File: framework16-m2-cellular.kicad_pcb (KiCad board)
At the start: 4 copper layers, 118.7 x 72.5 mm, 88 parts, among them J1 M.2 Socket B-Key (2199230-3), J10 MHF4L (20579-001E), J11 SIM Card, J12 Fan 1, J13 Fan 2, J2 u.FL, J3 MHF4L (20579-001E), J5 u.FL, J6 MHF4L (20579-001E), J7 u.FL, J8 MHF4L (20579-001E), J9 u.FL, Q1 NPN, U1 BR24G32FVT-3, U2 TCA9534, U3 74LVC1G11, U4 LTC6994xS6-1, U5 TPS628304ARZER

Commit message: Version v1.1
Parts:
- added R9: 1K, Resistor_SMD:R_0603_1608Metric, F.Cu at (119.2, 97.0)
- added TP11: TestPoint, TestPoint:TestPoint_Pad_D1.0mm, F.Cu at (104.0, 91.0)
- added TP12: TestPoint, TestPoint:TestPoint_Pad_D1.0mm, F.Cu at (114.0, 124.0)
- added TP15: TestPoint, TestPoint:TestPoint_Pad_D1.0mm, F.Cu at (110.0, 124.0)
- moved TP13 38.4 mm to (112.0, 124.0)
- moved U4 22.1 mm to (102.0, 94.2)
- moved C16 22.1 mm to (105.0, 94.2)
- moved R14 22.1 mm to (104.3, 96.7)
- moved R16 22.1 mm to (101.3, 96.7)
- moved R17 22.1 mm to (99.0, 95.2)
- moved TP10 16.7 mm to (98.5, 92.5)
- moved R23 12.6 mm to (160.5, 137.5), turned to -90 degrees
- moved D1 2.50 mm to (146.0, 83.4)
- moved D3 2.50 mm to (149.0, 83.4)
- moved R1 2.50 mm to (144.0, 83.7)
- moved R7 2.50 mm to (151.0, 83.7)
- moved TP4 1.00 mm to (104.5, 111.2)
- moved C21 0.75 mm to (108.8, 89.5)
- moved C22 0.75 mm to (113.5, 87.5)
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- renumbered R7 to R1, R9 to R10, R10 to R11, R11 to R12, R12 to R13, R13 to R14, R14 to R15, R15 to R16, R16 to R17, R17 to R18, R18 to R19, R19 to R20, R20 to R21, R21 to R22, R22 to R23, R23 to R24, R1 to R7, TP11 to TP13, TP12 to TP14
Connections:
- Q1 pad 1: /RESET -> Net-(Q1-B)
- R10 pad 1: /RESET -> Net-(Q1-B)
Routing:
- net Net-(J4-ID0): track 14.6 -> 2.62 mm, vias 2 -> 0
- net /MODEM_ON: track 95.2 -> 106.3 mm, vias 4 -> 5
- net Net-(J1-GPIO_9/DAS/~{DSS}/~{LED1}): track 40.9 -> 50.8 mm
- net +3.3V: track 194.2 -> 188.0 mm
- net GND: track 379.5 -> 383.7 mm, vias 7 -> 26
- net /RESET: track 30.9 -> 26.7 mm
- net Net-(Q1-B): track 0.00 -> 3.85 mm
- net Net-(J13-Pin_3): track 48.6 -> 50.9 mm
- net +3.7V_MODEM: track 118.5 -> 116.3 mm
- net /~{INT}: track 127.8 -> 129.7 mm
- net /RST: track 40.7 -> 42.6 mm
- net /D+: track 42.1 -> 43.8 mm, vias 2 -> 3
- net /D-: track 43.7 -> 45.4 mm, vias 2 -> 3
- net Net-(J12-Pin_3): track 51.5 -> 53.1 mm
- net Net-(J4-12V_FAN): track 19.3 -> 20.9 mm
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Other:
- board text added: "Framework 16 M.2 Cellular Module ${VERSION}"
- board text removed: "FW16 5G Module v1.0"

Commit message: Bunch of improvements for v1.1
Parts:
- added HS1: M.2 Thermal Pads, FW16Cellular:Thermal Pad, F.Cu at (186.0, 94.8)
- added HS1: M.2 Thermal Pads, FW16Cellular:Thermal Pad, F.Cu at (176.0, 113.8)
- added HS1: M.2 Thermal Pads, FW16Cellular:Thermal Pad, F.Cu at (186.0, 113.8)
- added HS1: M.2 Thermal Pads, FW16Cellular:Thermal Pad, F.Cu at (166.0, 104.2)
- added HS1: M.2 Thermal Pads, FW16Cellular:Thermal Pad, F.Cu at (156.0, 94.8)
- added HS1: M.2 Thermal Pads, FW16Cellular:Thermal Pad, F.Cu at (176.0, 94.8)
- added HS1: M.2 Thermal Pads, FW16Cellular:Thermal Pad, F.Cu at (166.0, 113.8)
- added HS1: M.2 Thermal Pads, FW16Cellular:Thermal Pad, F.Cu at (156.0, 113.8)
- added HS1: M.2 Thermal Pads, FW16Cellular:Thermal Pad, F.Cu at (166.0, 94.8)
- added HS1: M.2 Thermal Pads, FW16Cellular:Thermal Pad, F.Cu at (156.0, 104.2)
- J2, J5, J7, J9: value u.FL -> MHF4L (20579-001E); footprint FW16Cellular:CONN_U.FL-R-SMT10_HIR -> FW16Cellular:CONN_20579-001E_IPX
- moved J2 96.9 mm to (114.0, 72.5), turned to 0 degrees
- moved J5 92.9 mm to (120.0, 72.5), turned to 0 degrees
- moved J3 91.2 mm to (114.0, 75.0), turned to 180 degrees
- moved J7 89.7 mm to (126.0, 72.5), turned to 0 degrees
- moved J9 87.4 mm to (132.0, 72.5), turned to 0 degrees
- moved J6 87.1 mm to (120.0, 75.0), turned to 180 degrees
- moved J8 83.9 mm to (126.0, 75.0), turned to 180 degrees
- moved J10 81.6 mm to (132.0, 75.0), turned to 180 degrees
- moved D1 4.03 mm to (142.0, 83.9)
- moved D3 4.03 mm to (145.0, 83.9)
- moved R1 4.03 mm to (140.0, 84.2)
- moved R7 4.03 mm to (147.0, 84.2)
- moved H1 1.00 mm to (176.0, 104.2)
- moved H2 1.00 mm to (186.0, 104.2)
- moved L1 0.25 mm to (166.0, 126.5)
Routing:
- net GND: track 383.7 -> 351.5 mm
- net Net-(J1-GPIO_9/DAS/~{DSS}/~{LED1}): track 50.8 -> 37.9 mm
- net /VCC: track 51.9 -> 57.8 mm
- net /RST: track 42.6 -> 48.5 mm
- net /DATA: track 39.1 -> 44.9 mm
- net /CLK: track 38.5 -> 44.4 mm
- net /~{CLKREQ}: track 46.3 -> 51.6 mm
- net /~{RST}: track 43.6 -> 47.1 mm
- net /MODEM_ON: track 106.3 -> 109.6 mm
- net /~{W_DISABLE1}: track 58.6 -> 61.7 mm
- net /REFCLKP: track 62.0 -> 64.9 mm
- net /REFCLKN: track 62.0 -> 64.9 mm
- net Net-(J1-~{FULL_CARD_POWER_OFF}): track 51.6 -> 54.2 mm
- net /~{INT}: track 129.7 -> 128.5 mm
- net +3.7V_MODEM: track 116.3 -> 115.0 mm
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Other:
- board text added: "EC ON"
- board text added: "FW Laptop 16 Expansion Bay M.2 5G Module ${VERSION}"
- board text removed: "Framework 16 M.2 Cellular Module ${VERSION}"

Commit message: Fixes from v1.1
TODO: check the orientation of the fan headers
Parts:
- C13, C5: footprint Capacitor_SMD:CP_Elec_8x10 -> Capacitor_SMD:CP_Elec_6.3x5.4
- J12, J13: footprint FW16Cellular:A1001WR-S-04P -> FW16Cellular:AFC30-S04FCC-00
- moved C5 0.25 mm to (126.0, 120.0)
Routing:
- net GND: track 351.5 -> 339.2 mm
- net +12V_FAN: track 104.4 -> 105.9 mm
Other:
- board text added: "EC CTRL"
- board text removed: "EC ON"

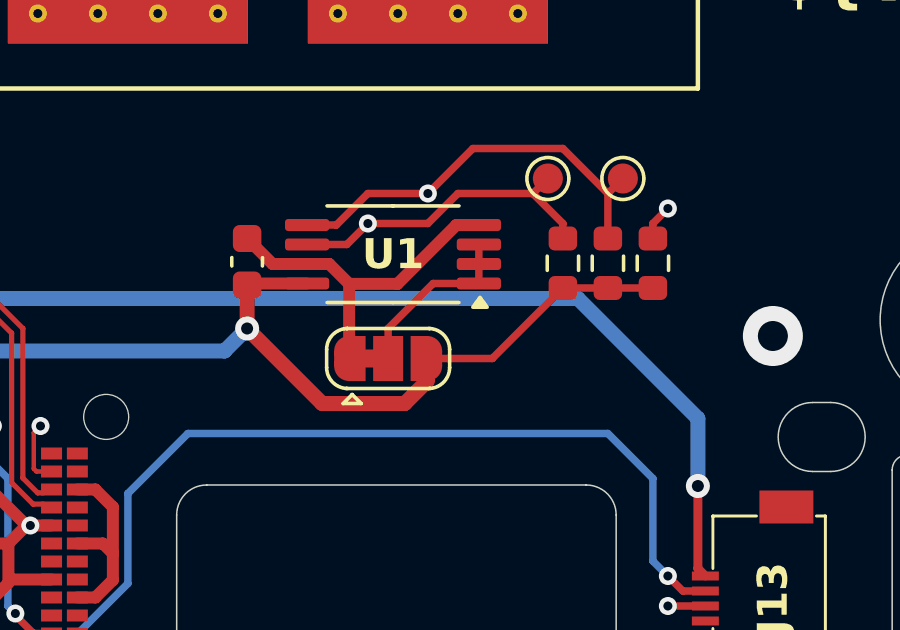
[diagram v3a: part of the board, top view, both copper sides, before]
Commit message: Remove EEPROM address jumper
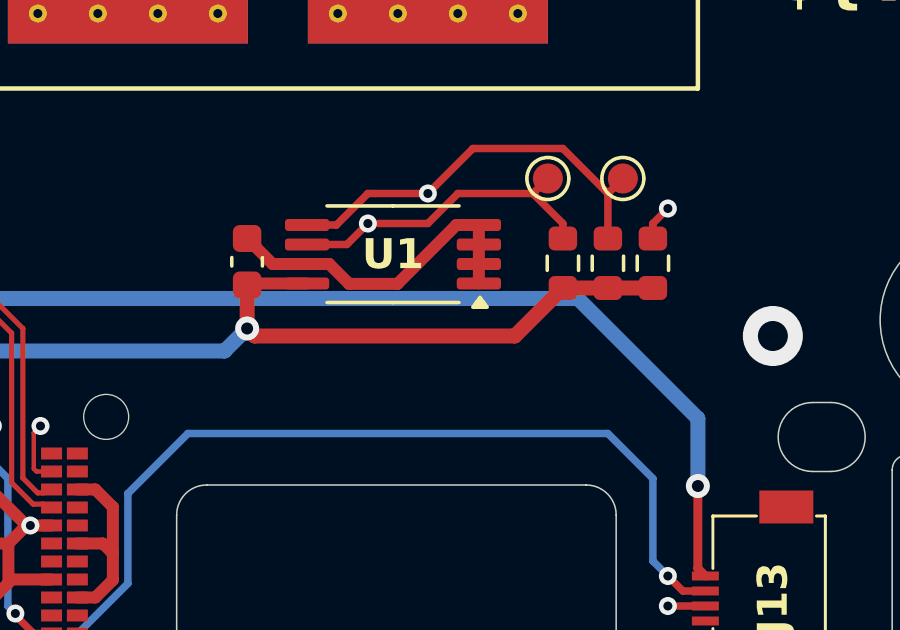
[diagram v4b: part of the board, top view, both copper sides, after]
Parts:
- removed the JP1 at (184.7, 128.2)
- renumbered JP2 to JP1
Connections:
- U1 pad 1: Net-(JP1-C) (its old number) -> GND
- U1 pad 2: Net-(JP1-C) (its old number) -> GND
- U1 pad 3: Net-(JP1-C) (its old number) -> GND
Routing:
- net Net-(JP1-C) (its old number): track 5.95 -> 0.00 mm
- net +3.3V: track 188.6 -> 186.4 mm
- net GND: track 339.2 -> 338.7 mm

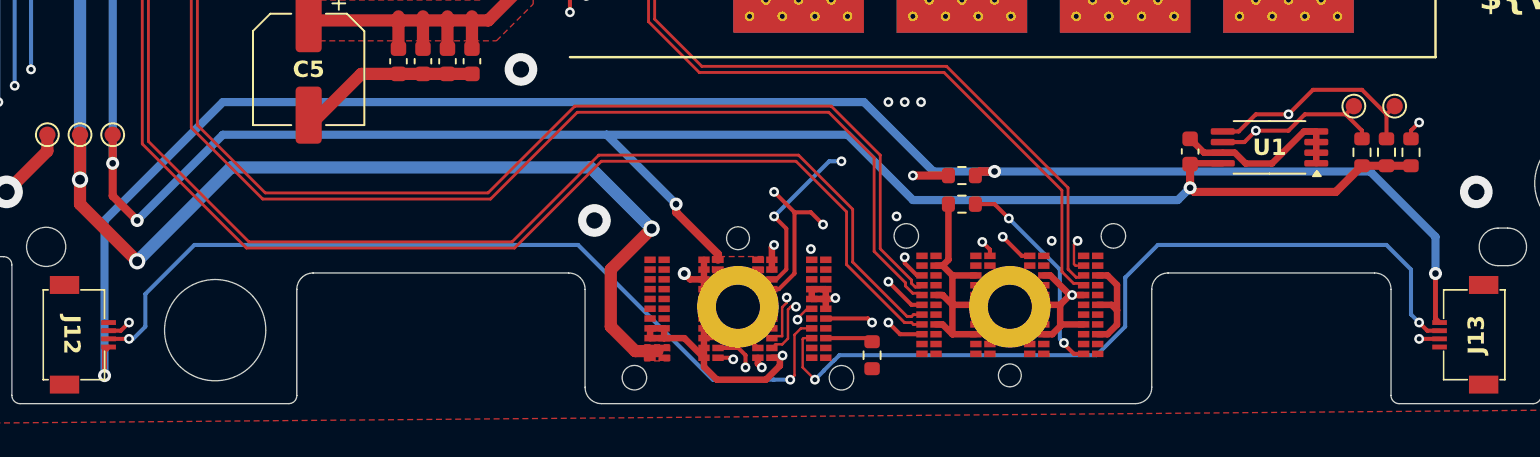
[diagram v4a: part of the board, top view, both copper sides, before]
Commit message: Fix flipped fan connector
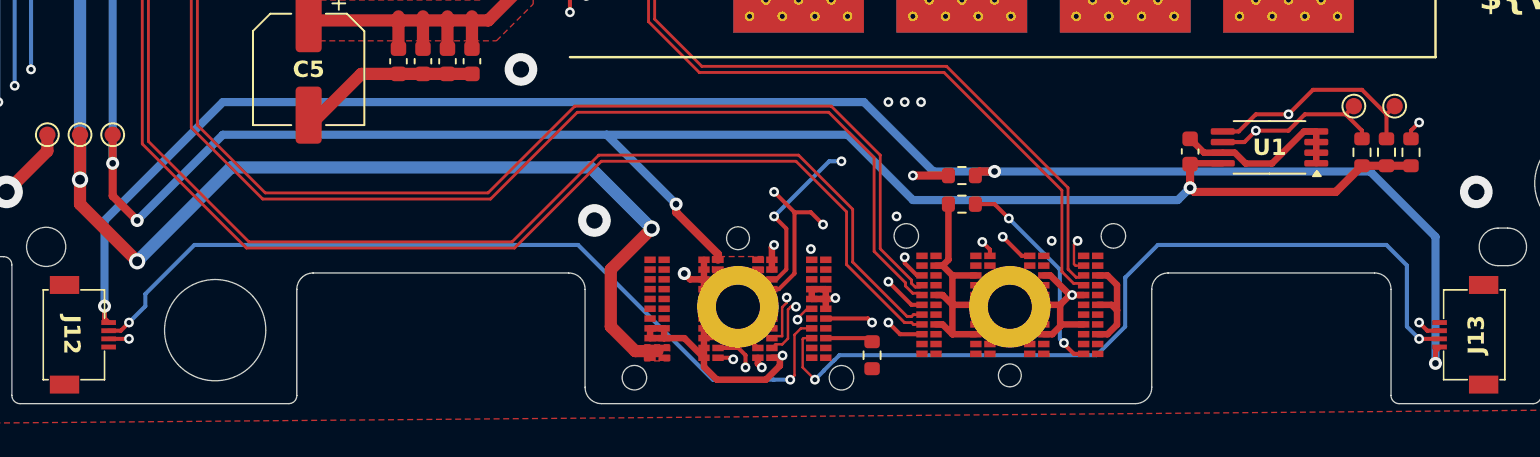
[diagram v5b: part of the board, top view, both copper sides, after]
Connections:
- J12 pad 1: GND -> +12V_FAN
- J12 pad 4: +12V_FAN -> GND
- J13 pad 1: GND -> +12V_FAN
- J13 pad 4: +12V_FAN -> GND
- J4 pad PH2: Net-(J12-Pin_3) -> Net-(J12-Pin_2)
- J4 pad PJ2: Net-(J13-Pin_3) -> Net-(J13-Pin_2)
- J4 pad PK5: Net-(J13-Pin_2) -> Net-(J13-Pin_3)
- J4 pad PL5: Net-(J12-Pin_2) -> Net-(J12-Pin_3)
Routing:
- net Net-(J12-Pin_3): track 52.8 -> 45.5 mm
- net Net-(J12-Pin_2): track 44.9 -> 51.9 mm
- net Net-(J13-Pin_2): track 56.4 -> 51.4 mm
- net Net-(J13-Pin_3): track 50.6 -> 54.4 mm
- net +12V_FAN: track 105.9 -> 104.4 mm
